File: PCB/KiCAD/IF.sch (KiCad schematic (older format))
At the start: 34 parts, among them J2 JACK_TRS_3pins, P4 CONN_01X01, P5 CONN_01X01, P6 CONN_01X01, P7 CONN_01X01, Q6 MMBFJ310LT1G, U1 NE5532, U4 LM78L06, U5 SA612

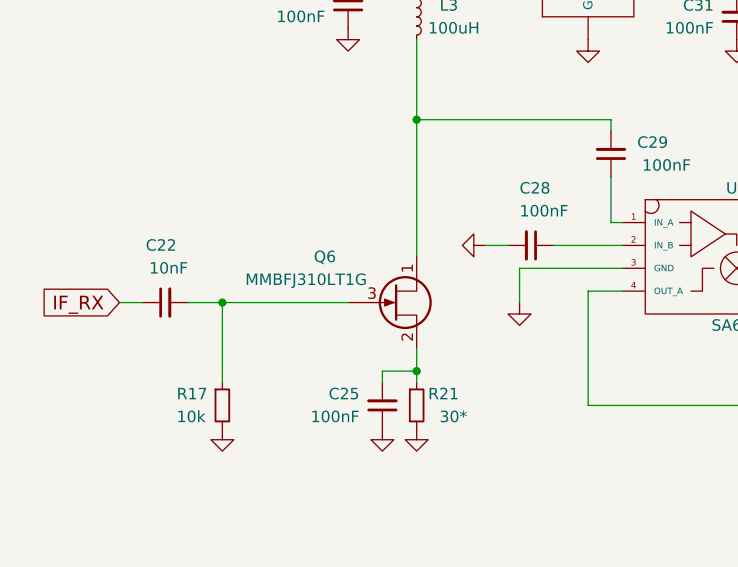
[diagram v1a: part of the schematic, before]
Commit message: PCB progress, fix MMBFJ310 error
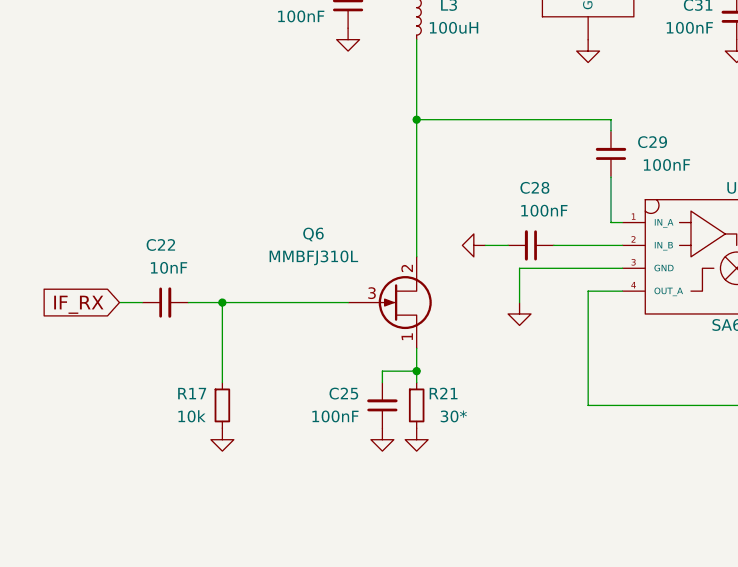
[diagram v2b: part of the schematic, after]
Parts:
- removed Q6: MMBFJ310LT1G, DragonFly:SOT-23, symbol Q_NJFET_SDG
- added Q6: MMBFJ310L, DragonFly:SOT-23, symbol Q_NJFET_DSG
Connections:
- net at C29.2, L3.2: now also Q6.2 (S)
- net at C25.2, R21.1: now also Q6.1 (D)
- net at C22.2, R17.1: now also Q6.3 (G)
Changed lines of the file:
@@
 $EndComp
 $Comp
-L GND #PWR053
+L GND #PWR69
 U 1 1 58912103
 P 7700 2550
-F 0 "#PWR053" H 7700 2300 50  0001 C CNN
+F 0 "#PWR69" H 7700 2300 50  0001 C CNN
 F 1 "GND" H 7700 2400 50  0001 C CNN
 F 2 "" H 7700 2550 50  0000 C CNN
@@
 $EndComp
 $Comp
-L GND #PWR054
+L GND #PWR70
 U 1 1 58912546
 P 7700 2750
-F 0 "#PWR054" H 7700 2500 50  0001 C CNN
+F 0 "#PWR70" H 7700 2500 50  0001 C CNN
 F 1 "GND" H 7700 2600 50  0001 C CNN
 F 2 "" H 7700 2750 50  0000 C CNN
@@
 $EndComp
 $Comp
-L GND #PWR055
+L GND #PWR71
 U 1 1 58912989
 P 7700 2950
-F 0 "#PWR055" H 7700 2700 50  0001 C CNN
+F 0 "#PWR71" H 7700 2700 50  0001 C CNN
 F 1 "GND" H 7700 2800 50  0001 C CNN
 F 2 "" H 7700 2950 50  0000 C CNN
@@
 $EndComp
 $Comp
-L GND #PWR056
+L GND #PWR72
 U 1 1 589132CC
 P 7700 3150
-F 0 "#PWR056" H 7700 2900 50  0001 C CNN
+F 0 "#PWR72" H 7700 2900 50  0001 C CNN
 F 1 "GND" H 7700 3000 50  0001 C CNN
 F 2 "" H 7700 3150 50  0000 C CNN
@@
 $EndComp
 $Comp
-L GND #PWR057
+L GND #PWR59
 U 1 1 58AF70A6
 P 3000 3300
-F 0 "#PWR057" H 3000 3050 50  0001 C CNN
+F 0 "#PWR59" H 3000 3050 50  0001 C CNN
 F 1 "GND" H 3000 3150 50  0001 C CNN
 F 2 "" H 3000 3300 50  0000 C CNN
@@
 $EndComp
 $Comp
-L GND #PWR058
+L GND #PWR56
 U 1 1 58B15E5F
 P 2250 5000
-F 0 "#PWR058" H 2250 4750 50  0001 C CNN
+F 0 "#PWR56" H 2250 4750 50  0001 C CNN
 F 1 "GND" H 2250 4850 50  0001 C CNN
 F 2 "" H 2250 5000 50  0000 C CNN
@@
 $EndComp
 $Comp
-L GND #PWR059
+L GND #PWR53
 U 1 1 58B0B2EB
 P 1400 5000
-F 0 "#PWR059" H 1400 4750 50  0001 C CNN
+F 0 "#PWR53" H 1400 4750 50  0001 C CNN
 F 1 "GND" H 1400 4850 50  0001 C CNN
 F 2 "" H 1400 5000 50  0000 C CNN
@@
 $EndComp
 $Comp
-L GND #PWR060
+L GND #PWR54
 U 1 1 58B0BE25
 P 1950 3250
-F 0 "#PWR060" H 1950 3000 50  0001 C CNN
+F 0 "#PWR54" H 1950 3000 50  0001 C CNN
 F 1 "GND" H 1950 3100 50  0001 C CNN
 F 2 "" H 1950 3250 50  0000 C CNN
@@
 $EndComp
 $Comp
-L Q_NJFET_SDG Q6
-U 1 1 58AFFBB6
-P 2150 4450
-F 0 "Q6" H 1800 4250 50  0000 L CNN
-F 1 "MMBFJ310LT1G" H 1500 4350 50  0000 L CNN
-F 2 "DragonFly:SOT-23" H -4600 200 50  0001 C CNN
-F 3 "" H -4800 100 50  0001 C CNN
-	1    2150 4450
-	1    0    0    1
-$EndComp
-$Comp
 L R_Small R21
 U 1 1 58B01EBA
@@
 $EndComp
 $Comp
-L GND #PWR061
+L GND #PWR55
 U 1 1 58B02D08
 P 2100 5000
-F 0 "#PWR061" H 2100 4750 50  0001 C CNN
+F 0 "#PWR55" H 2100 4750 50  0001 C CNN
 F 1 "GND" H 2100 4850 50  0001 C CNN
 F 2 "" H 2100 5000 50  0000 C CNN
@@
 $EndComp
 $Comp
-L GND #PWR062
+L GND #PWR58
 U 1 1 58B09A3F
 P 2700 4450
-F 0 "#PWR062" H 2700 4200 50  0001 C CNN
+F 0 "#PWR58" H 2700 4200 50  0001 C CNN
 F 1 "GND" H 2700 4300 50  0001 C CNN
 F 2 "" H 2700 4450 50  0000 C CNN
@@
 $EndComp
 $Comp
-L GND #PWR063
+L GND #PWR60
 U 1 1 58B399E4
 P 3650 3300
-F 0 "#PWR063" H 3650 3050 50  0001 C CNN
+F 0 "#PWR60" H 3650 3050 50  0001 C CNN
 F 1 "GND" H 3650 3150 50  0001 C CNN
 F 2 "" H 3650 3300 50  0000 C CNN
@@
 $EndComp
 $Comp
-L GND #PWR064
+L GND #PWR61
 U 1 1 58B39C92
 P 3850 3300
-F 0 "#PWR064" H 3850 3050 50  0001 C CNN
+F 0 "#PWR61" H 3850 3050 50  0001 C CNN
 F 1 "GND" H 3850 3150 50  0001 C CNN
 F 2 "" H 3850 3300 50  0000 C CNN
@@
 $EndComp
 $Comp
-L GND #PWR065
+L GND #PWR57
 U 1 1 58B3CA01
 P 2550 4200
-F 0 "#PWR065" H 2550 3950 50  0001 C CNN
+F 0 "#PWR57" H 2550 3950 50  0001 C CNN
 F 1 "GND" H 2550 4050 50  0001 C CNN
 F 2 "" H 2550 4200 50  0000 C CNN
@@
 $EndComp
 $Comp
-L GND #PWR066
+L GND #PWR63
 U 1 1 60FB6B9C
 P 4900 3500
-F 0 "#PWR066" H 4900 3250 50  0001 C CNN
+F 0 "#PWR63" H 4900 3250 50  0001 C CNN
 F 1 "GND" H 4900 3350 50  0001 C CNN
 F 2 "" H 4900 3500 50  0000 C CNN
@@
 $EndComp
 $Comp
-L GND #PWR067
+L GND #PWR62
 U 1 1 60FB7F45
 P 4550 4200
-F 0 "#PWR067" H 4550 3950 50  0001 C CNN
+F 0 "#PWR62" H 4550 3950 50  0001 C CNN
 F 1 "GND" H 4550 4050 50  0001 C CNN
 F 2 "" H 4550 4200 50  0000 C CNN
@@
 $EndComp
 $Comp
-L GND #PWR068
+L GND #PWR74
 U 1 1 60FB9C6F
 P 9550 5600
-F 0 "#PWR068" H 9550 5350 50  0001 C CNN
+F 0 "#PWR74" H 9550 5350 50  0001 C CNN
 F 1 "GND" H 9550 5450 50  0001 C CNN
 F 2 "" H 9550 5600 50  0000 C CNN
@@
 Connection ~ 6700 5000
 $Comp
-L GND #PWR069
+L GND #PWR73
 U 1 1 6123D132
 P 7850 5400
-F 0 "#PWR069" H 7850 5150 50  0001 C CNN
+F 0 "#PWR73" H 7850 5150 50  0001 C CNN
 F 1 "GND" H 7850 5250 50  0001 C CNN
 F 2 "" H 7850 5400 50  0000 C CNN
@@
 $EndComp
 $Comp
-L GND #PWR070
+L GND #PWR64
 U 1 1 61240985
 P 4950 5250
-F 0 "#PWR070" H 4950 5000 50  0001 C CNN
+F 0 "#PWR64" H 4950 5000 50  0001 C CNN
 F 1 "GND" H 4950 5100 50  0001 C CNN
 F 2 "" H 4950 5250 50  0000 C CNN
@@
 $EndComp
 $Comp
-L GND #PWR071
+L GND #PWR67
 U 1 1 61240A0C
 P 5600 5300
-F 0 "#PWR071" H 5600 5050 50  0001 C CNN
+F 0 "#PWR67" H 5600 5050 50  0001 C CNN
 F 1 "GND" H 5600 5150 50  0001 C CNN
 F 2 "" H 5600 5300 50  0000 C CNN
@@
 Connection ~ 7200 4900
 $Comp
-L GND #PWR072
+L GND #PWR68
 U 1 1 61241D9A
 P 7200 5200
-F 0 "#PWR072" H 7200 4950 50  0001 C CNN
+F 0 "#PWR68" H 7200 4950 50  0001 C CNN
 F 1 "GND" H 7200 5050 50  0001 C CNN
 F 2 "" H 7200 5200 50  0000 C CNN
@@
 	5250 5850 5250 5950
 $Comp
-L GND #PWR073
+L GND #PWR66
 U 1 1 61243457
 P 5250 6350
-F 0 "#PWR073" H 5250 6100 50  0001 C CNN
+F 0 "#PWR66" H 5250 6100 50  0001 C CNN
 F 1 "GND" H 5250 6200 50  0001 C CNN
 F 2 "" H 5250 6350 50  0000 C CNN
@@
 	7850 4550 7850 4700
 $Comp
-L GND #PWR074
+L GND #PWR65
 U 1 1 61244C87
 P 5100 4550
-F 0 "#PWR074" H 5100 4300 50  0001 C CNN
+F 0 "#PWR65" H 5100 4300 50  0001 C CNN
 F 1 "GND" H 5100 4400 50  0001 C CNN
 F 2 "" H 5100 4550 50  0000 C CNN
@@
 	3850 3100 3850 3000
 Connection ~ 3850 3000
+$Comp
+L Q_NJFET_DSG Q6
+U 1 1 612A9C34
+P 2150 4450
+F 0 "Q6" H 1750 4150 50  0000 L CNN
+F 1 "MMBFJ310L" H 1600 4250 50  0000 L CNN
+F 2 "DragonFly:SOT-23" H 2350 4550 50  0001 C CNN
+F 3 "" H 2150 4450 50  0001 C CNN
+	1    2150 4450
+	1    0    0    1
+$EndComp
 $EndSCHEMATC
